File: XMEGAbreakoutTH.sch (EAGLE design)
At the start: 24 parts, among them IC1 XMEGA16A4

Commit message: eagle layout finished
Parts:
- JP1: device SparkFun:M08 -> SparkFun:M081X08_2X1X4A
- JP2, JP3, JP5: device SparkFun:M08SMD-STRAIGHT-ALT -> SparkFun:M081X08
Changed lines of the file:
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@@
 <parts>
 <part name="IC1" library="atmel" deviceset="XMEGA16A4" device="" value="XMEGA16A4"/>
-<part name="JP2" library="SparkFun" deviceset="M08" device="SMD-STRAIGHT-ALT"/>
-<part name="JP3" library="SparkFun" deviceset="M08" device="SMD-STRAIGHT-ALT"/>
+<part name="JP2" library="SparkFun" deviceset="M08" device="1X08"/>
+<part name="JP3" library="SparkFun" deviceset="M08" device="1X08"/>
 <part name="C1" library="fab" deviceset="CAP-US" device="1206" value="0.1uF"/>
 <part name="C2" library="fab" deviceset="CAP-US" device="1206" value="10uF"/>
@@
 <part name="GND2" library="SparkFun" deviceset="GND" device=""/>
 <part name="GND3" library="SparkFun" deviceset="GND" device=""/>
-<part name="JP5" library="SparkFun" deviceset="M08" device="SMD-STRAIGHT-ALT"/>
-<part name="JP1" library="SparkFun" deviceset="M08" device=""/>
+<part name="JP5" library="SparkFun" deviceset="M08" device="1X08"/>
+<part name="JP1" library="SparkFun" deviceset="M08" device="1X08_2X1X4A"/>
 <part name="GND4" library="SparkFun" deviceset="GND" device=""/>
 <part name="P+3" library="SparkFun" deviceset="VCC" device=""/>

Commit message: small changes
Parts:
- added C5: 4.7uF, fab:CAP-US1206
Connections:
- net GND: now also C5.2
- net VBUS: now also C5.1
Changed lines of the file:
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@@
 <grid distance="0.1" unitdist="inch" unit="inch" style="lines" multiple="1" display="no" altdistance="0.01" altunitdist="inch" altunit="inch"/>
 <layers>
-<layer number="1" name="Top" color="4" fill="1" visible="yes" active="no"/>
-<layer number="2" name="Route2" color="1" fill="3" visible="yes" active="no"/>
-<layer number="3" name="Route3" color="4" fill="3" visible="yes" active="no"/>
-<layer number="14" name="Route14" color="1" fill="6" visible="yes" active="no"/>
-<layer number="15" name="Route15" color="4" fill="6" visible="yes" active="no"/>
-<layer number="16" name="Bottom" color="1" fill="1" visible="yes" active="no"/>
-<layer number="17" name="Pads" color="2" fill="1" visible="yes" active="no"/>
-<layer number="18" name="Vias" color="2" fill="1" visible="yes" active="no"/>
-<layer number="19" name="Unrouted" color="6" fill="1" visible="yes" active="no"/>
-<layer number="20" name="Dimension" color="15" fill="1" visible="yes" active="no"/>
-<layer number="21" name="tPlace" color="7" fill="1" visible="yes" active="no"/>
-<layer number="22" name="bPlace" color="7" fill="1" visible="yes" active="no"/>
-<layer number="23" name="tOrigins" color="15" fill="1" visible="yes" active="no"/>
-<layer number="24" name="bOrigins" color="15" fill="1" visible="yes" active="no"/>
-<layer number="25" name="tNames" color="7" fill="1" visible="yes" active="no"/>
-<layer number="26" name="bNames" color="7" fill="1" visible="yes" active="no"/>
-<layer number="27" name="tValues" color="7" fill="1" visible="yes" active="no"/>
-<layer number="28" name="bValues" color="7" fill="1" visible="yes" active="no"/>
+<layer number="1" name="Top" color="4" fill="1" visible="no" active="no"/>
+<layer number="2" name="Route2" color="1" fill="3" visible="no" active="no"/>
+<layer number="3" name="Route3" color="4" fill="3" visible="no" active="no"/>
+<layer number="14" name="Route14" color="1" fill="6" visible="no" active="no"/>
+<layer number="15" name="Route15" color="4" fill="6" visible="no" active="no"/>
+<layer number="16" name="Bottom" color="1" fill="1" visible="no" active="no"/>
+<layer number="17" name="Pads" color="2" fill="1" visible="no" active="no"/>
+<layer number="18" name="Vias" color="2" fill="1" visible="no" active="no"/>
+<layer number="19" name="Unrouted" color="6" fill="1" visible="no" active="no"/>
+<layer number="20" name="Dimension" color="15" fill="1" visible="no" active="no"/>
+<layer number="21" name="tPlace" color="7" fill="1" visible="no" active="no"/>
+<layer number="22" name="bPlace" color="7" fill="1" visible="no" active="no"/>
+<layer number="23" name="tOrigins" color="15" fill="1" visible="no" active="no"/>
+<layer number="24" name="bOrigins" color="15" fill="1" visible="no" active="no"/>
+<layer number="25" name="tNames" color="7" fill="1" visible="no" active="no"/>
+<layer number="26" name="bNames" color="7" fill="1" visible="no" active="no"/>
+<layer number="27" name="tValues" color="7" fill="1" visible="no" active="no"/>
+<layer number="28" name="bValues" color="7" fill="1" visible="no" active="no"/>
 <layer number="29" name="tStop" color="7" fill="3" visible="no" active="no"/>
 <layer number="30" name="bStop" color="7" fill="6" visible="no" active="no"/>
@@
 <layer number="35" name="tGlue" color="7" fill="4" visible="no" active="no"/>
 <layer number="36" name="bGlue" color="7" fill="5" visible="no" active="no"/>
-<layer number="37" name="tTest" color="7" fill="1" visible="yes" active="no"/>
-<layer number="38" name="bTest" color="7" fill="1" visible="yes" active="no"/>
+<layer number="37" name="tTest" color="7" fill="1" visible="no" active="no"/>
+<layer number="38" name="bTest" color="7" fill="1" visible="no" active="no"/>
 <layer number="39" name="tKeepout" color="4" fill="11" visible="no" active="no"/>
 <layer number="40" name="bKeepout" color="1" fill="11" visible="no" active="no"/>
@@
 <layer number="44" name="Drills" color="7" fill="1" visible="no" active="no"/>
 <layer number="45" name="Holes" color="7" fill="1" visible="no" active="no"/>
-<layer number="46" name="Milling" color="3" fill="1" visible="yes" active="no"/>
-<layer number="47" name="Measures" color="7" fill="1" visible="yes" active="no"/>
-<layer number="48" name="Document" color="7" fill="1" visible="yes" active="no"/>
-<layer number="49" name="Reference" color="7" fill="1" visible="yes" active="no"/>
-<layer number="50" name="dxf" color="7" fill="1" visible="yes" active="no"/>
-<layer number="51" name="tDocu" color="7" fill="1" visible="yes" active="no"/>
-<layer number="52" name="bDocu" color="7" fill="1" visible="yes" active="no"/>
-<layer number="53" name="tGND_GNDA" color="7" fill="9" visible="yes" active="no"/>
-<layer number="54" name="bGND_GNDA" color="1" fill="9" visible="yes" active="no"/>
-<layer number="56" name="wert" color="7" fill="1" visible="yes" active="no"/>
+<layer number="46" name="Milling" color="3" fill="1" visible="no" active="no"/>
+<layer number="47" name="Measures" color="7" fill="1" visible="no" active="no"/>
+<layer number="48" name="Document" color="7" fill="1" visible="no" active="no"/>
+<layer number="49" name="Reference" color="7" fill="1" visible="no" active="no"/>
+<layer number="50" name="dxf" color="7" fill="1" visible="no" active="no"/>
+<layer number="51" name="tDocu" color="7" fill="1" visible="no" active="no"/>
+<layer number="52" name="bDocu" color="7" fill="1" visible="no" active="no"/>
+<layer number="53" name="tGND_GNDA" color="7" fill="9" visible="no" active="no"/>
+<layer number="54" name="bGND_GNDA" color="1" fill="9" visible="no" active="no"/>
+<layer number="56" name="wert" color="7" fill="1" visible="no" active="no"/>
 <layer number="90" name="Modules" color="5" fill="1" visible="yes" active="yes"/>
 <layer number="91" name="Nets" color="2" fill="1" visible="yes" active="yes"/>
@@
 <part name="JUMPER1" library="fab" deviceset="RES-US" device="1206FAB" value="0"/>
 <part name="JUMPER2" library="fab" deviceset="RES-US" device="1206FAB" value="0"/>
+<part name="C5" library="fab" deviceset="CAP-US" device="1206" value="4.7uF"/>
 </parts>
 <sheets>
@@
 <instance part="JUMPER1" gate="G$1" x="0" y="175.26"/>
 <instance part="JUMPER2" gate="G$1" x="0" y="167.64"/>
+<instance part="C5" gate="G$1" x="30.48" y="162.56" rot="R270"/>
 </instances>
 <busses>
@@
 <wire x1="53.34" y1="170.18" x2="43.18" y2="170.18" width="0.1524" layer="91"/>
 <wire x1="43.18" y1="170.18" x2="43.18" y2="167.64" width="0.1524" layer="91"/>
-<wire x1="43.18" y1="170.18" x2="27.94" y2="170.18" width="0.1524" layer="91"/>
+<wire x1="43.18" y1="170.18" x2="30.48" y2="170.18" width="0.1524" layer="91"/>
 <junction x="43.18" y="170.18"/>
 <label x="27.94" y="170.18" size="1.778" layer="95"/>
+<pinref part="C5" gate="G$1" pin="1"/>
+<wire x1="30.48" y1="170.18" x2="27.94" y2="170.18" width="0.1524" layer="91"/>
+<wire x1="30.48" y1="165.1" x2="30.48" y2="170.18" width="0.1524" layer="91"/>
+<junction x="30.48" y="170.18"/>
 </segment>
 <segment>
@@
 <wire x1="106.68" y1="147.32" x2="106.68" y2="144.78" width="0.1524" layer="91"/>
 <junction x="96.52" y="147.32"/>
-</segment>
-</net>
+<pinref part="C5" gate="G$1" pin="2"/>
+<wire x1="30.48" y1="157.48" x2="30.48" y2="147.32" width="0.1524" layer="91"/>
+<wire x1="30.48" y1="147.32" x2="43.18" y2="147.32" width="0.1524" layer="91"/>
+<junction x="43.18" y="147.32"/>
+</segment>
+</net>

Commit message: diode array
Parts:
- removed D1, D2, D3, D4, D5: (no value), fab:ZENER_DIODESOD123
- added U$2: INVERTER, SparkFun:INVERTER
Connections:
- net D+: now also U$2.GND; no longer D2.ANODE, D3.CATHODE
- net D-: now also U$2.Y; no longer D1.ANODE, D4.CATHODE
- net GND: now also U$2.A
- net N$25: no longer D3.ANODE, D4.ANODE, D5.ANODE
- net VBUS: now also U$2.VCC; no longer D1.CATHODE, D2.CATHODE, D5.CATHODE

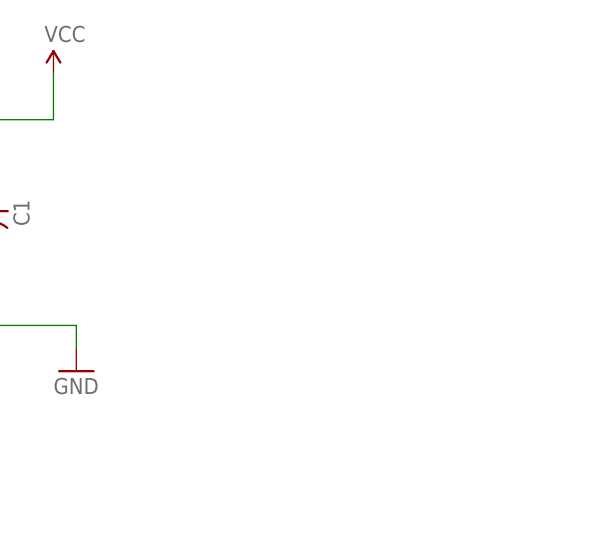
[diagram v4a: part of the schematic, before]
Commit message: added power pins
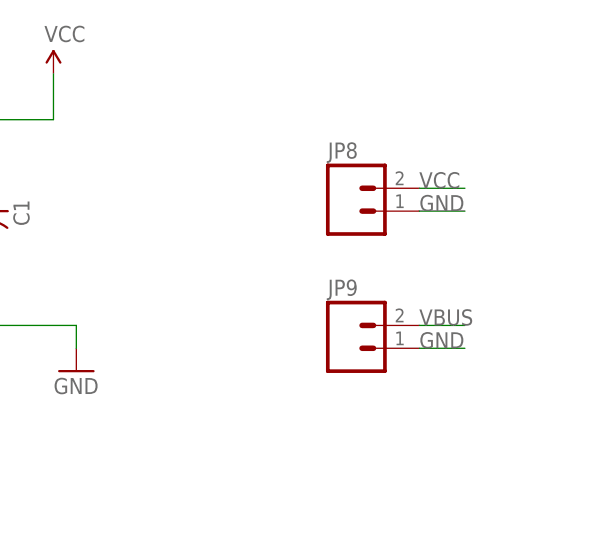
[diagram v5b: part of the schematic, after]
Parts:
- added JP8, JP9: (no value), SparkFun:M02PTH
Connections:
- net GND: now also JP8.1, JP9.1
- net VBUS: now also JP9.2
- net VCC: now also JP8.2
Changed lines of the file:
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@@
 <grid distance="0.1" unitdist="inch" unit="inch" style="lines" multiple="1" display="no" altdistance="0.01" altunitdist="inch" altunit="inch"/>
 <layers>
-<layer number="1" name="Top" color="4" fill="1" visible="yes" active="no"/>
-<layer number="2" name="Route2" color="1" fill="3" visible="yes" active="no"/>
-<layer number="3" name="Route3" color="4" fill="3" visible="yes" active="no"/>
-<layer number="14" name="Route14" color="1" fill="6" visible="yes" active="no"/>
-<layer number="15" name="Route15" color="4" fill="6" visible="yes" active="no"/>
-<layer number="16" name="Bottom" color="1" fill="1" visible="yes" active="no"/>
-<layer number="17" name="Pads" color="2" fill="1" visible="yes" active="no"/>
-<layer number="18" name="Vias" color="2" fill="1" visible="yes" active="no"/>
-<layer number="19" name="Unrouted" color="6" fill="1" visible="yes" active="no"/>
-<layer number="20" name="Dimension" color="15" fill="1" visible="yes" active="no"/>
-<layer number="21" name="tPlace" color="7" fill="1" visible="yes" active="no"/>
-<layer number="22" name="bPlace" color="7" fill="1" visible="yes" active="no"/>
-<layer number="23" name="tOrigins" color="15" fill="1" visible="yes" active="no"/>
-<layer number="24" name="bOrigins" color="15" fill="1" visible="yes" active="no"/>
-<layer number="25" name="tNames" color="7" fill="1" visible="yes" active="no"/>
-<layer number="26" name="bNames" color="7" fill="1" visible="yes" active="no"/>
-<layer number="27" name="tValues" color="7" fill="1" visible="yes" active="no"/>
-<layer number="28" name="bValues" color="7" fill="1" visible="yes" active="no"/>
+<layer number="1" name="Top" color="4" fill="1" visible="no" active="no"/>
+<layer number="2" name="Route2" color="1" fill="3" visible="no" active="no"/>
+<layer number="3" name="Route3" color="4" fill="3" visible="no" active="no"/>
+<layer number="14" name="Route14" color="1" fill="6" visible="no" active="no"/>
+<layer number="15" name="Route15" color="4" fill="6" visible="no" active="no"/>
+<layer number="16" name="Bottom" color="1" fill="1" visible="no" active="no"/>
+<layer number="17" name="Pads" color="2" fill="1" visible="no" active="no"/>
+<layer number="18" name="Vias" color="2" fill="1" visible="no" active="no"/>
+<layer number="19" name="Unrouted" color="6" fill="1" visible="no" active="no"/>
+<layer number="20" name="Dimension" color="15" fill="1" visible="no" active="no"/>
+<layer number="21" name="tPlace" color="7" fill="1" visible="no" active="no"/>
+<layer number="22" name="bPlace" color="7" fill="1" visible="no" active="no"/>
+<layer number="23" name="tOrigins" color="15" fill="1" visible="no" active="no"/>
+<layer number="24" name="bOrigins" color="15" fill="1" visible="no" active="no"/>
+<layer number="25" name="tNames" color="7" fill="1" visible="no" active="no"/>
+<layer number="26" name="bNames" color="7" fill="1" visible="no" active="no"/>
+<layer number="27" name="tValues" color="7" fill="1" visible="no" active="no"/>
+<layer number="28" name="bValues" color="7" fill="1" visible="no" active="no"/>
 <layer number="29" name="tStop" color="7" fill="3" visible="no" active="no"/>
 <layer number="30" name="bStop" color="7" fill="6" visible="no" active="no"/>
@@
 <layer number="35" name="tGlue" color="7" fill="4" visible="no" active="no"/>
 <layer number="36" name="bGlue" color="7" fill="5" visible="no" active="no"/>
-<layer number="37" name="tTest" color="7" fill="1" visible="yes" active="no"/>
-<layer number="38" name="bTest" color="7" fill="1" visible="yes" active="no"/>
+<layer number="37" name="tTest" color="7" fill="1" visible="no" active="no"/>
+<layer number="38" name="bTest" color="7" fill="1" visible="no" active="no"/>
 <layer number="39" name="tKeepout" color="4" fill="11" visible="no" active="no"/>
 <layer number="40" name="bKeepout" color="1" fill="11" visible="no" active="no"/>
@@
 <layer number="44" name="Drills" color="7" fill="1" visible="no" active="no"/>
 <layer number="45" name="Holes" color="7" fill="1" visible="no" active="no"/>
-<layer number="46" name="Milling" color="3" fill="1" visible="yes" active="no"/>
-<layer number="47" name="Measures" color="7" fill="1" visible="yes" active="no"/>
-<layer number="48" name="Document" color="7" fill="1" visible="yes" active="no"/>
-<layer number="49" name="Reference" color="7" fill="1" visible="yes" active="no"/>
-<layer number="50" name="dxf" color="7" fill="1" visible="yes" active="no"/>
-<layer number="51" name="tDocu" color="7" fill="1" visible="yes" active="no"/>
-<layer number="52" name="bDocu" color="7" fill="1" visible="yes" active="no"/>
-<layer number="53" name="tGND_GNDA" color="7" fill="9" visible="yes" active="no"/>
-<layer number="54" name="bGND_GNDA" color="1" fill="9" visible="yes" active="no"/>
-<layer number="56" name="wert" color="7" fill="1" visible="yes" active="no"/>
+<layer number="46" name="Milling" color="3" fill="1" visible="no" active="no"/>
+<layer number="47" name="Measures" color="7" fill="1" visible="no" active="no"/>
+<layer number="48" name="Document" color="7" fill="1" visible="no" active="no"/>
+<layer number="49" name="Reference" color="7" fill="1" visible="no" active="no"/>
+<layer number="50" name="dxf" color="7" fill="1" visible="no" active="no"/>
+<layer number="51" name="tDocu" color="7" fill="1" visible="no" active="no"/>
+<layer number="52" name="bDocu" color="7" fill="1" visible="no" active="no"/>
+<layer number="53" name="tGND_GNDA" color="7" fill="9" visible="no" active="no"/>
+<layer number="54" name="bGND_GNDA" color="1" fill="9" visible="no" active="no"/>
+<layer number="56" name="wert" color="7" fill="1" visible="no" active="no"/>
 <layer number="90" name="Modules" color="5" fill="1" visible="yes" active="yes"/>
 <layer number="91" name="Nets" color="2" fill="1" visible="yes" active="yes"/>
@@
 <part name="C5" library="fab" deviceset="CAP-US" device="1206" value="4.7uF"/>
 <part name="U$2" library="SparkFun" deviceset="INVERTER" device=""/>
+<part name="JP8" library="SparkFun" deviceset="M02" device="PTH"/>
+<part name="JP9" library="SparkFun" deviceset="M02" device="PTH"/>
 </parts>
 <sheets>
@@
 <instance part="C5" gate="G$1" x="30.48" y="162.56" rot="R270"/>
 <instance part="U$2" gate="G$1" x="30.48" y="116.84"/>
+<instance part="JP8" gate="G$1" x="137.16" y="160.02"/>
+<instance part="JP9" gate="G$1" x="137.16" y="144.78"/>
 </instances>
 <busses>
@@
 <wire x1="40.64" y1="121.92" x2="50.8" y2="121.92" width="0.1524" layer="91"/>
 <label x="45.72" y="121.92" size="1.778" layer="95"/>
+</segment>
+<segment>
+<pinref part="JP9" gate="G$1" pin="2"/>
+<wire x1="144.78" y1="147.32" x2="149.86" y2="147.32" width="0.1524" layer="91"/>
+<label x="144.78" y="147.32" size="1.778" layer="95"/>
 </segment>
 </net>
@@
 <label x="7.62" y="116.84" size="1.778" layer="95"/>
 </segment>
+<segment>
+<pinref part="JP8" gate="G$1" pin="1"/>
+<wire x1="144.78" y1="160.02" x2="149.86" y2="160.02" width="0.1524" layer="91"/>
+<label x="144.78" y="160.02" size="1.778" layer="95"/>
+</segment>
+<segment>
+<pinref part="JP9" gate="G$1" pin="1"/>
+<wire x1="144.78" y1="144.78" x2="149.86" y2="144.78" width="0.1524" layer="91"/>
+<label x="144.78" y="144.78" size="1.778" layer="95"/>
+</segment>
 </net>
 <net name="VCC" class="0">
@@
 <junction x="96.52" y="170.18"/>
 </segment>
-</net>
+<segment>
+<pinref part="JP8" gate="G$1" pin="2"/>
+<wire x1="144.78" y1="162.56" x2="149.86" y2="162.56" width="0.1524" layer="91"/>
+<label x="144.78" y="162.56" size="1.778" layer="95"/>
+</segment>
+</net>
